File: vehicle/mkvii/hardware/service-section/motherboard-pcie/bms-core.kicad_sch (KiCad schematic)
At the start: 1 part, among them J801 pcie_x1

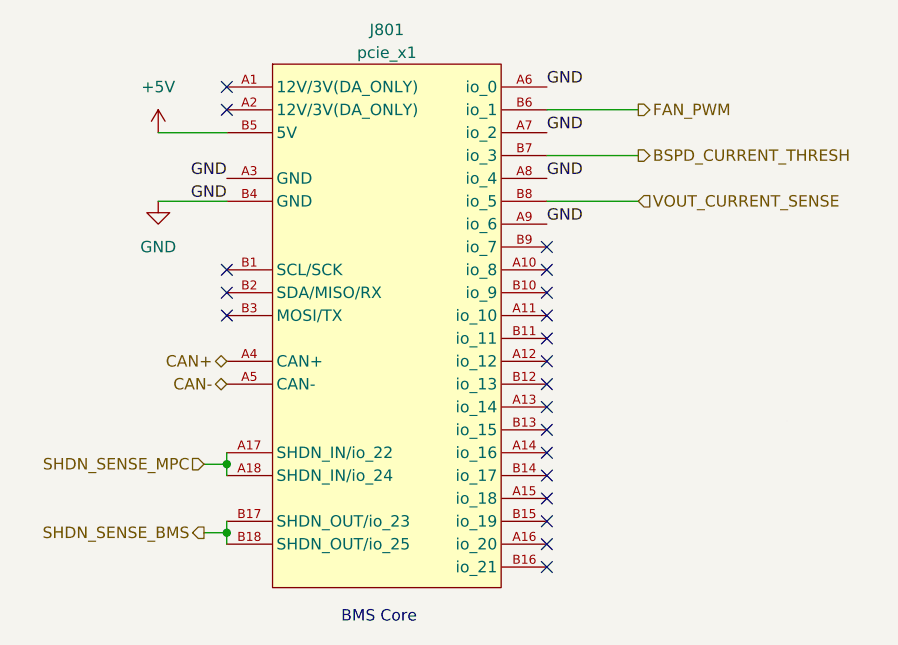
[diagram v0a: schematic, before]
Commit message: changed values of connectors, added edge cuts of other boards and motherboard, added buck converter
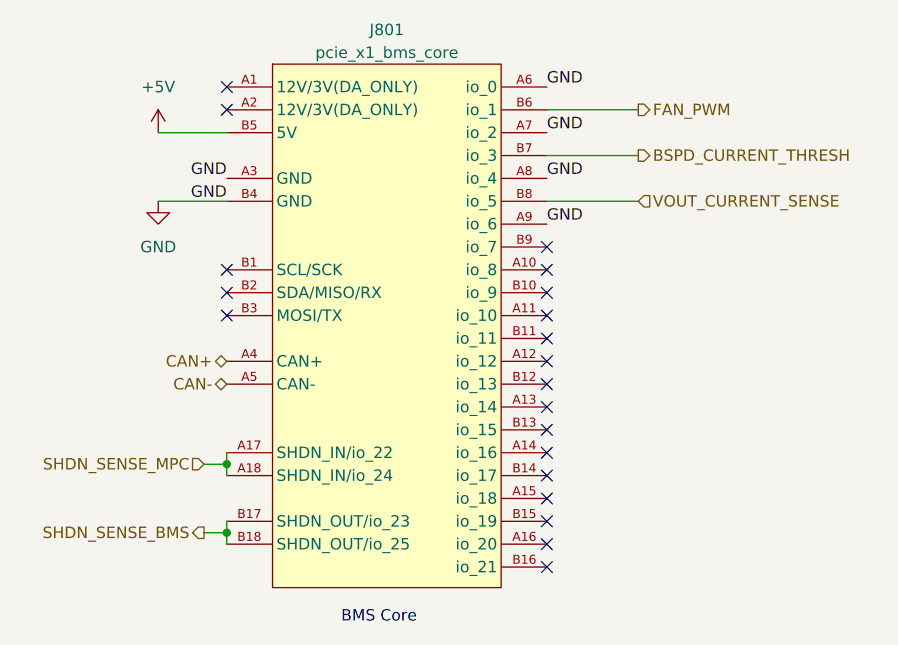
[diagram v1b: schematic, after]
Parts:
- J801: value pcie_x1 -> pcie_x1_bms_core
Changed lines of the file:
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@@
 			)
 		)
-		(property "Value" "pcie_x1"
+		(property "Value" "pcie_x1_bms_core"
 			(at 142.24 69.85 0)
 			(do_not_autoplace yes)

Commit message: routed everything LV thats not power; moved bms orientation and position, created shutdown loop
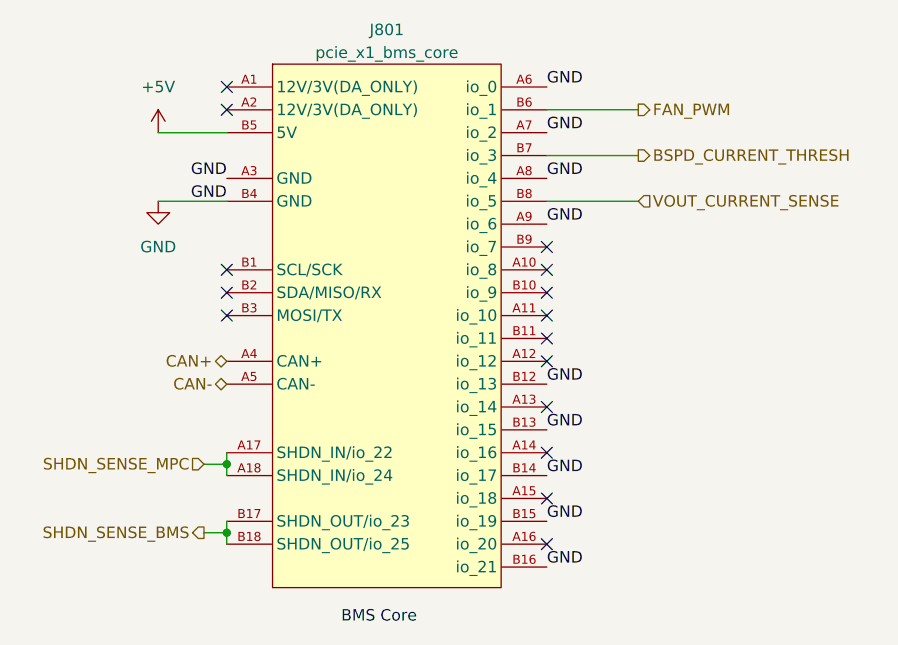
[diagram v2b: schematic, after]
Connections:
- net GND: now also J801.B12 (io_13), J801.B13 (io_15), J801.B14 (io_17), J801.B15 (io_19), J801.B16 (io_21)
- no-connect marks 20 -> 15
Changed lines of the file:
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@@
-	)
-	(no_connect
-		(at 160.02 106.68)
 	)
 	(no_connect
@@
 	)
 	(no_connect
-		(at 160.02 116.84)
-	)
-	(no_connect
-		(at 160.02 127)
-	)
-	(no_connect
-		(at 160.02 111.76)
-	)
-	(no_connect
 		(at 160.02 91.44)
 	)
@@
 	(no_connect
 		(at 160.02 109.22)
-	)
-	(no_connect
-		(at 160.02 121.92)
 	)
 	(wire
@@
 	)
 	(label "GND"
+		(at 160.02 111.76 0)
+		(fields_autoplaced yes)
+		(effects
+			(font
+				(size 1.27 1.27)
+			)
+			(justify left bottom)
+		)
+	)
+	(label "GND"
+		(at 160.02 121.92 0)
+		(fields_autoplaced yes)
+		(effects
+			(font
+				(size 1.27 1.27)
+			)
+			(justify left bottom)
+		)
+	)
+	(label "GND"
 		(at 160.02 73.66 0)
 		(fields_autoplaced yes)
@@
 		(fields_autoplaced yes)
 		(effects
+			(font
+				(size 1.27 1.27)
+			)
+			(justify left bottom)
+		)
+	)
+	(label "GND"
+		(at 160.02 106.68 0)
+		(fields_autoplaced yes)
+		(effects
+			(font
+				(size 1.27 1.27)
+			)
+			(justify left bottom)
+		)
+	)
+	(label "GND"
+		(at 160.02 116.84 0)
+		(fields_autoplaced yes)
+		(effects
+			(font
+				(size 1.27 1.27)
+			)
+			(justify left bottom)
+		)
+	)
+	(label "GND"
+		(at 160.02 127 0)
+		(fields_autoplaced yes)
+		(effects

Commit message: added precharge discharge update, correct precharge, bms, and air ctrl pinouts (swap CAN- and CAN+ for AIRCTRL), added decor
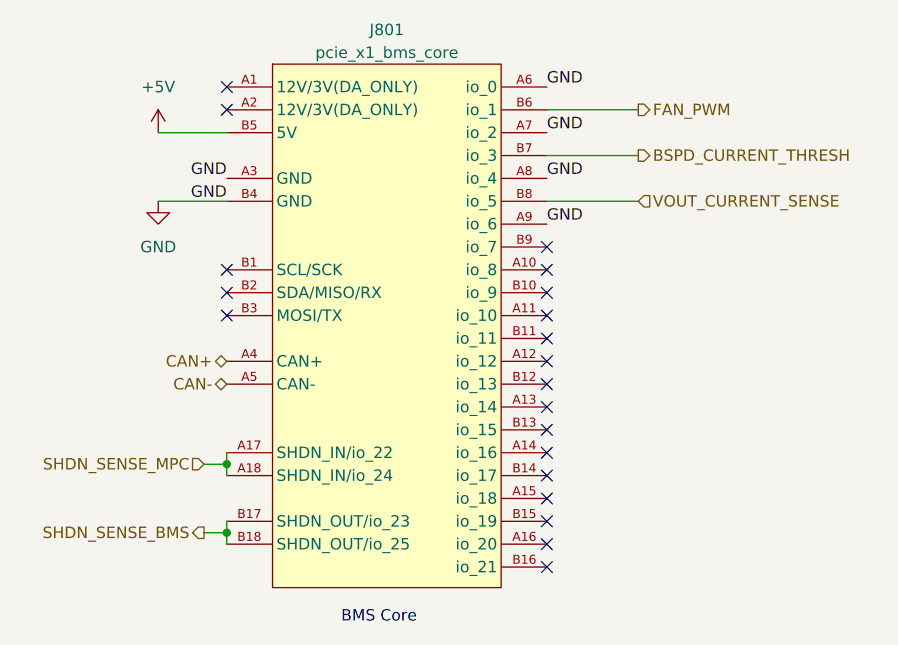
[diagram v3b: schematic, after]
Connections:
- net GND: no longer J801.B12 (io_13), J801.B13 (io_15), J801.B14 (io_17), J801.B15 (io_19), J801.B16 (io_21)
- no-connect marks 15 -> 20
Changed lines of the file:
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@@
+	)
+	(no_connect
+		(at 160.02 127)
+	)
+	(no_connect
+		(at 160.02 116.84)
 	)
 	(no_connect
 		(at 160.02 93.98)
+	)
+	(no_connect
+		(at 160.02 121.92)
 	)
 	(no_connect
@@
 	)
 	(no_connect
+		(at 160.02 106.68)
+	)
+	(no_connect
 		(at 160.02 91.44)
 	)
 	(no_connect
 		(at 124.46 99.06)
+	)
+	(no_connect
+		(at 160.02 111.76)
 	)
 	(no_connect
@@
 	)
 	(label "GND"
-		(at 160.02 111.76 0)
-		(fields_autoplaced yes)
-		(effects
-			(font
-				(size 1.27 1.27)
-			)
-			(justify left bottom)
-		)
-	)
-	(label "GND"
-		(at 160.02 121.92 0)
-		(fields_autoplaced yes)
-		(effects
-			(font
-				(size 1.27 1.27)
-			)
-			(justify left bottom)
-		)
-	)
-	(label "GND"
 		(at 160.02 73.66 0)
 		(fields_autoplaced yes)
@@
 		(fields_autoplaced yes)
 		(effects
-			(font
-				(size 1.27 1.27)
-			)
-			(justify left bottom)
-		)
-	)
-	(label "GND"
-		(at 160.02 106.68 0)
-		(fields_autoplaced yes)
-		(effects
-			(font
-				(size 1.27 1.27)
-			)
-			(justify left bottom)
-		)
-	)
-	(label "GND"
-		(at 160.02 116.84 0)
-		(fields_autoplaced yes)
-		(effects
-			(font
-				(size 1.27 1.27)
-			)
-			(justify left bottom)
-		)
-	)
-	(label "GND"
-		(at 160.02 127 0)
-		(fields_autoplaced yes)
-		(effects
